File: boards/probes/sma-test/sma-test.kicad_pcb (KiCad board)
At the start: 4 copper layers, 45.6 x 44.1 mm, 6 parts, among them J1 901-10511-3, J2 901-10510-2, J3 901-10309, J4 901-10511-3, J5 901-10510-2, J6 901-10309

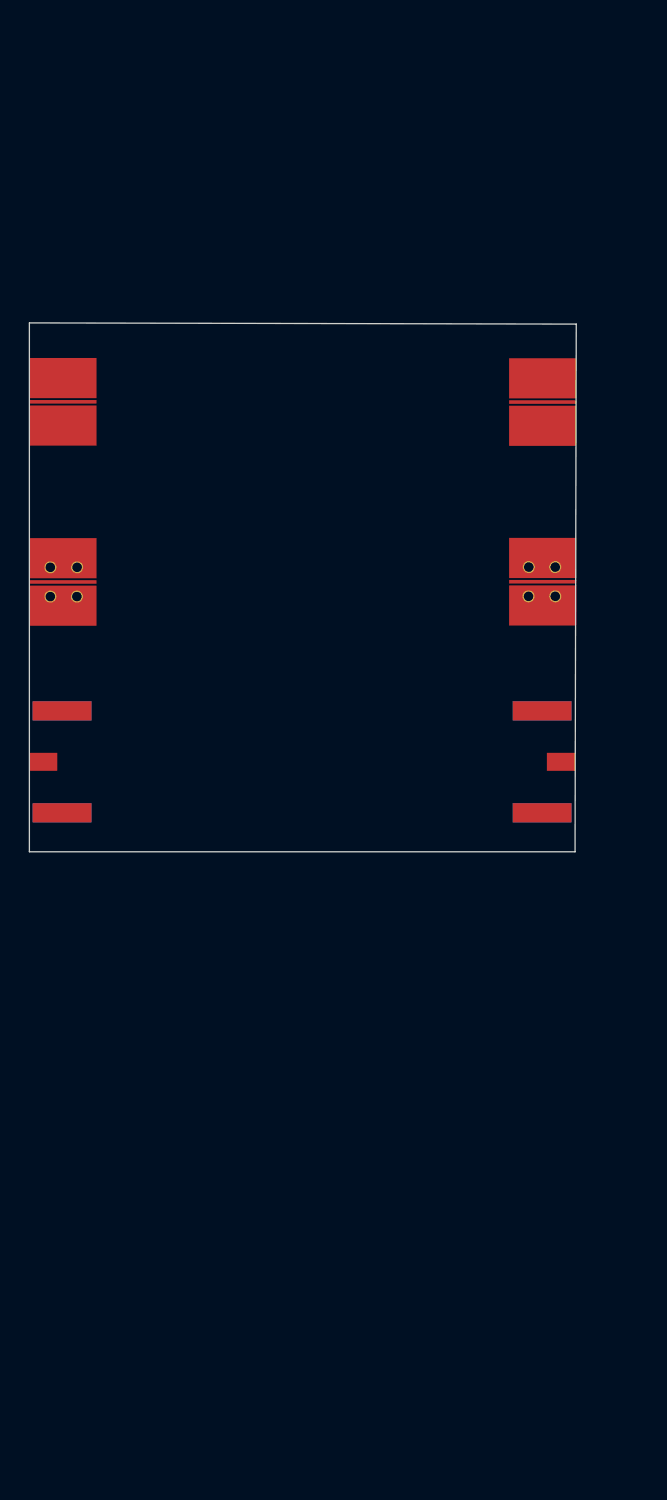
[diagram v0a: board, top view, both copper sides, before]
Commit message: Final version of sma-test board for fab
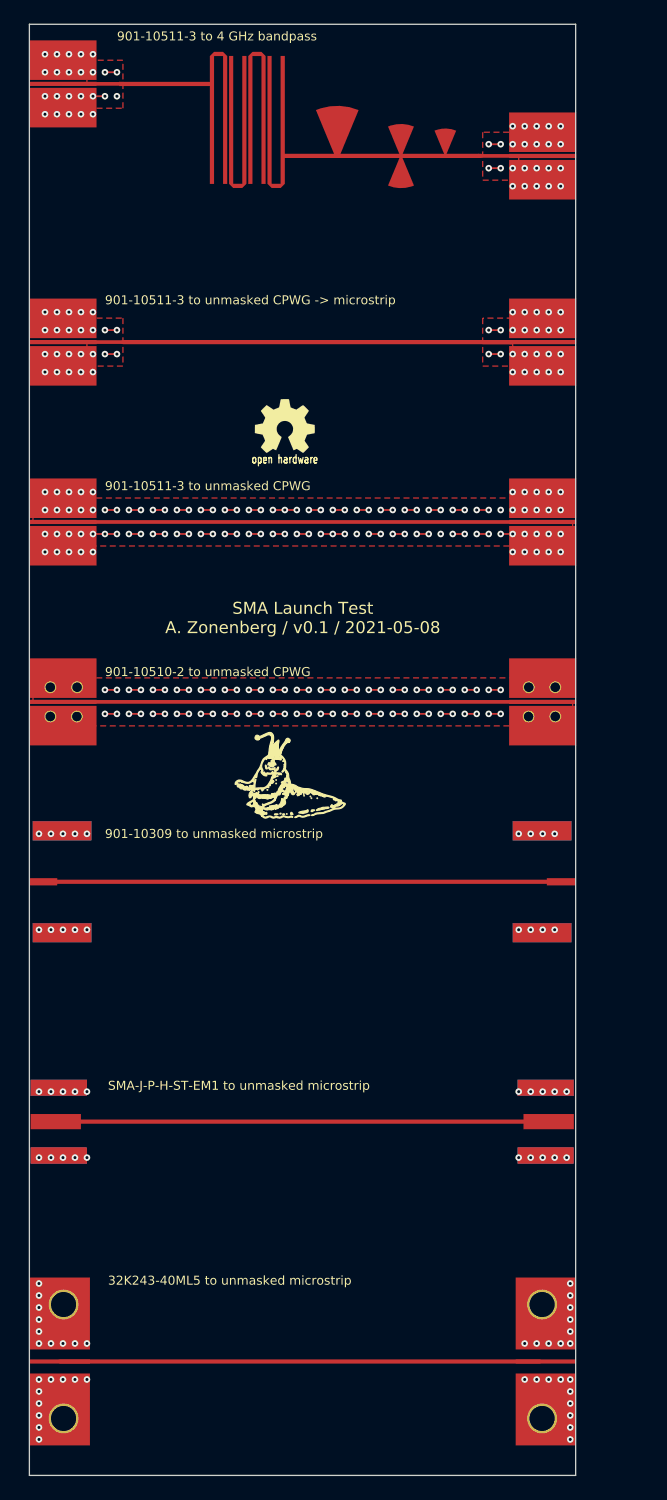
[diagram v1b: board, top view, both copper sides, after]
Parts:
- added FL1: FILTER, sma-test:filter2, F.Cu at (69.0, 29.8)
- added G***: LOGO, azonenberg_pcb:LONGTHING-1200DPI, F.Cu at (70.0, 82.0)
- added G***: LOGO, w_logo:Logo_silk_OSHW_6x6mm, F.Cu at (69.0, 52.5)
- added J10: 901-10511-3, azonenberg_pcb:CONN_SMA_EDGE_AMPHENOL_901_10511_3, F.Cu at (50.5, 24.0)
- added J11: SMA-J-P-H-ST-EM1, azonenberg_pcb:CONN_SMA_EDGE_SAMTEC_SMA_J_P_H_ST_EM1, F.Cu at (47.8, 110.5)
- added J12: 32K243-40ML5, azonenberg_pcb:CONN_SMA_EDGE_ROSENBERGER_32K243_40ML5, F.Cu at (47.8, 130.5)
- added J13: SMA-J-P-H-ST-EM1, azonenberg_pcb:CONN_SMA_EDGE_SAMTEC_SMA_J_P_H_ST_EM1, F.Cu at (93.1, 110.5)
- added J14: 32K243-40ML5, azonenberg_pcb:CONN_SMA_EDGE_ROSENBERGER_32K243_40ML5, F.Cu at (93.2, 130.5)
- added J7: 901-10511-3, azonenberg_pcb:CONN_SMA_EDGE_AMPHENOL_901_10511_3, F.Cu at (50.5, 45.5)
- added J8: 901-10511-3, azonenberg_pcb:CONN_SMA_EDGE_AMPHENOL_901_10511_3, F.Cu at (90.5, 45.5)
- added J9: 901-10511-3, azonenberg_pcb:CONN_SMA_EDGE_AMPHENOL_901_10511_3, F.Cu at (90.5, 30.0)
- moved J5 10.0 mm to (93.3, 75.5)
- moved J1 10.0 mm to (50.5, 60.5)
- moved J2 10.0 mm to (47.7, 75.5)
- moved J3 10.0 mm to (47.7, 90.5)
- moved J4 10.0 mm to (90.5, 60.5)
- moved J6 10.0 mm to (93.2, 90.5)
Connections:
- J2 pad 1: /SIG1 -> /SIG2
- J3 pad 1: /SIG1 -> /SIG3
- J5 pad 1: /SIG1 -> /SIG2
- J6 pad 1: /SIG1 -> /SIG3
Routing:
- net /GND: track 0.00 -> 724.6 mm, vias 0 -> 350
- net /SIG4: track 0.00 -> 45.0 mm
- net /SIG3: track 0.00 -> 43.2 mm
- net /SIG6: track 0.00 -> 41.1 mm
- net /SIG1: track 0.00 -> 41.0 mm
- net /SIG7: track 0.00 -> 40.0 mm
- net /SIG2: track 0.00 -> 40.0 mm
- net /SIG5: track 0.00 -> 5.25 mm
- net /SIG5B: track 0.00 -> 4.88 mm
- added copper zone on F.Cu, net /GND
- added copper zone on In1.Cu, net /GND
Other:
- board size 45.6 x 44.1 mm -> 45.5 x 121 mm
- board text added: "32K243-40ML5 to unmasked microstrip"
- board text added: "901-10309 to unmasked microstrip"
- board text added: "901-10510-2 to unmasked CPWG"
- board text added: "901-10511-3 to 4 GHz bandpass"
- board text added: "901-10511-3 to unmasked CPWG"
- board text added: "901-10511-3 to unmasked CPWG -> microstrip"
- board text added: "SMA Launch Test A. Zonenberg / v0.1 / 2021-05-08"
- board text added: "SMA-J-P-H-ST-EM1 to unmasked microstrip"

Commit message: Updated sma-test board with new cutouts and Beatty standard
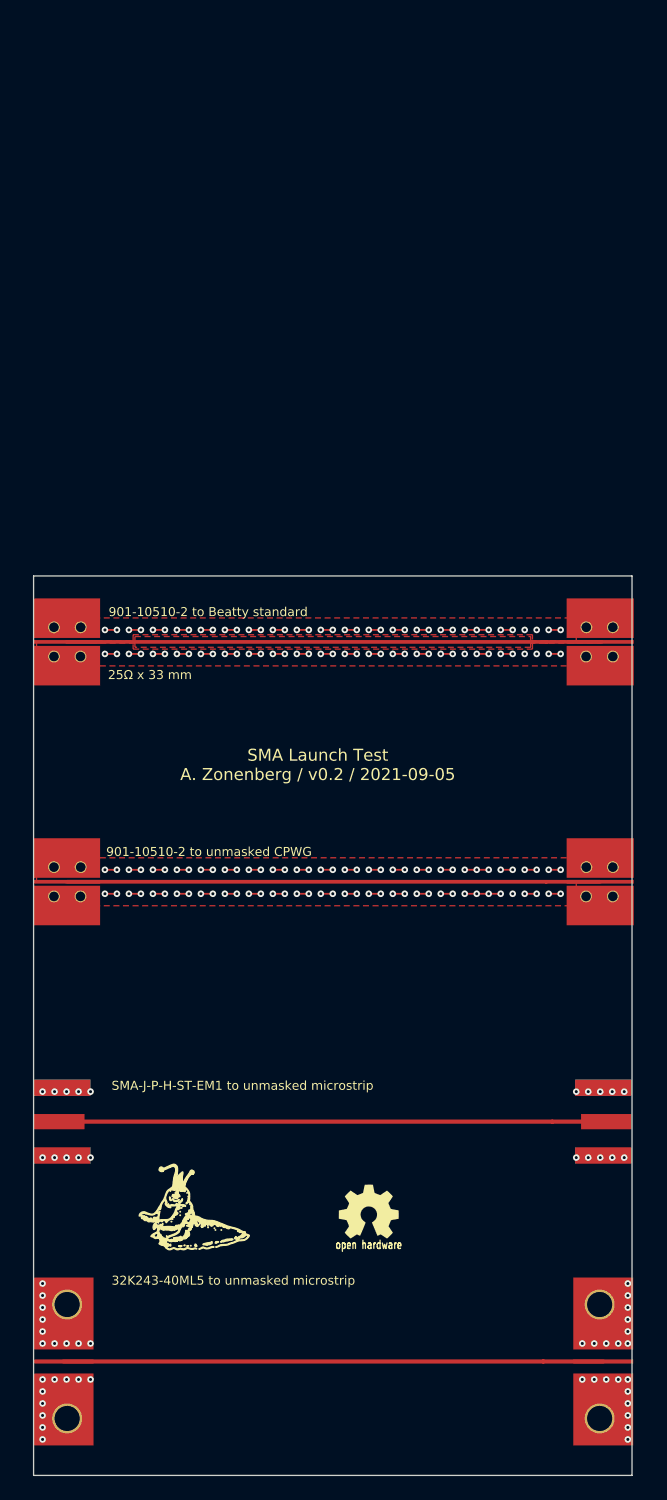
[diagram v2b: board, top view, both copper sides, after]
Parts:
- removed FL1: FILTER, sma-test:filter2
- removed J10, J4, J7, J8, J9: 901-10511-3, azonenberg_pcb:CONN_SMA_EDGE_AMPHENOL_901_10511_3
- removed J6: 901-10309, azonenberg_pcb:CONN_SMA_EDGE_AMPHENOL_901_10309
- J1: value 901-10511-3 -> 901-10510-2; footprint azonenberg_pcb:CONN_SMA_EDGE_AMPHENOL_901_10511_3 -> azonenberg_pcb:CONN_SMA_EDGE_AMPHENOL_901_10510-2
- J3: value 901-10309 -> 901-10510-2; footprint azonenberg_pcb:CONN_SMA_EDGE_AMPHENOL_901_10309 -> azonenberg_pcb:CONN_SMA_EDGE_AMPHENOL_901_10510-2
- moved G*** 65.9 mm to (76.0, 118.0)
- moved J3 54.2 mm to (98.1, 70.5), turned to 180 degrees
- moved G*** 36.9 mm to (62.0, 118.0)
- moved J5 15.7 mm to (98.1, 90.5)
- moved J2 15.0 mm to (48.0, 90.5)
- moved J1 10.3 mm to (48.0, 70.5)
- moved J13 4.80 mm to (97.9, 110.5)
- moved J14 4.80 mm to (98.0, 130.5)
- moved J11 0.30 mm to (48.1, 110.5)
- moved J12 0.30 mm to (48.0, 130.5)
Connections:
- J3 pad 1: /SIG3 -> /SIG1
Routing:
- net /GND: track 724.6 -> 426.8 mm, vias 350 -> 216
- net /SIG4: track 45.0 -> 0.00 mm
- net /SIG3: track 43.2 -> 0.00 mm
- net /SIG5: track 5.25 -> 0.00 mm
- net /SIG7: track 40.0 -> 45.0 mm
- net /SIG5B: track 4.88 -> 0.00 mm
- net /SIG2: track 40.0 -> 44.5 mm
- net /SIG6: track 41.1 -> 45.6 mm
- net /SIG1: track 41.0 -> 44.5 mm
- added copper zone on F.Cu, net /SIG1
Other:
- board size 45.5 x 121 mm -> 49.9 x 75 mm
- board text added: "25Ω x 33 mm"
- board text added: "901-10510-2 to Beatty standard"
- board text added: "SMA Launch Test A. Zonenberg / v0.2 / 2021-09-05"
- board text removed: "901-10309 to unmasked microstrip"
- board text removed: "901-10511-3 to 4 GHz bandpass"
- board text removed: "901-10511-3 to unmasked CPWG"
- board text removed: "901-10511-3 to unmasked CPWG -> microstrip"
- board text removed: "SMA Launch Test A. Zonenberg / v0.1 / 2021-05-08"

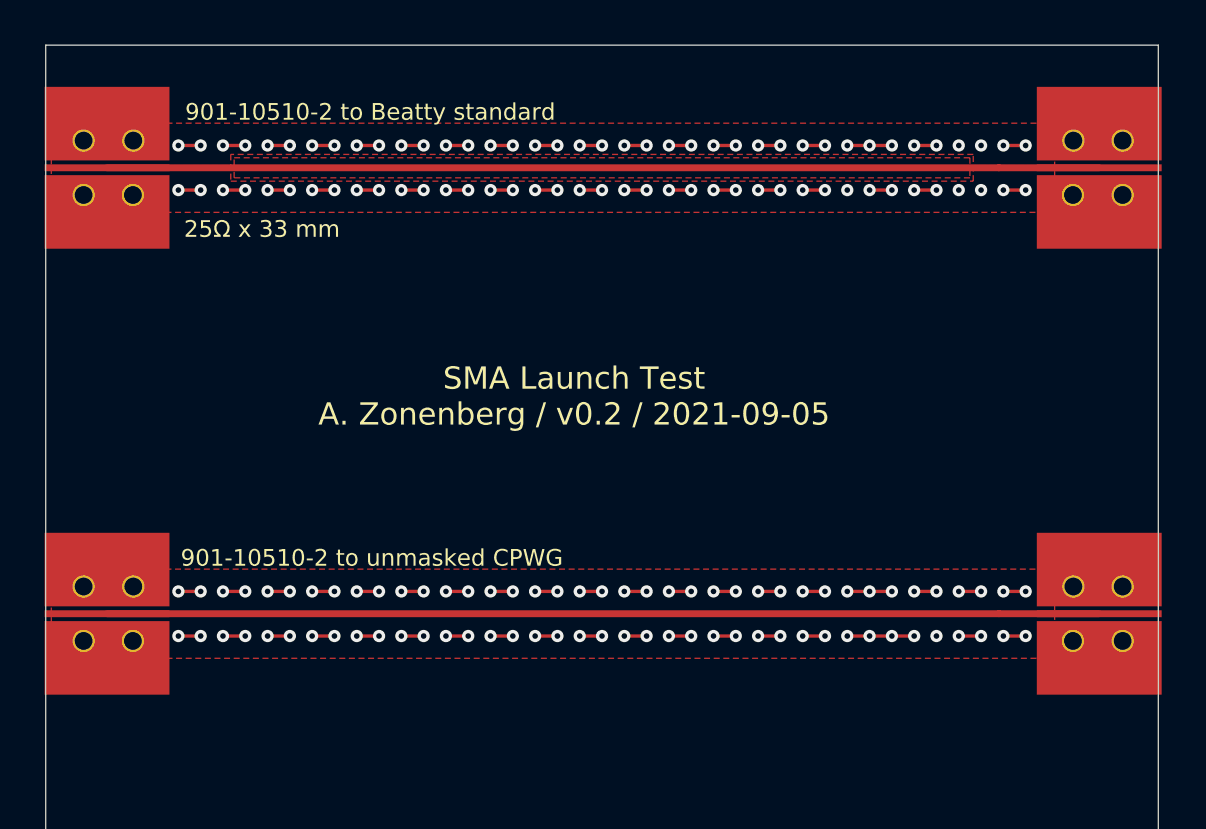
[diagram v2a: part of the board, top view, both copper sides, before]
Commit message: Updated 901-10510-2 with latest footprint from library. Added more vias to connector field
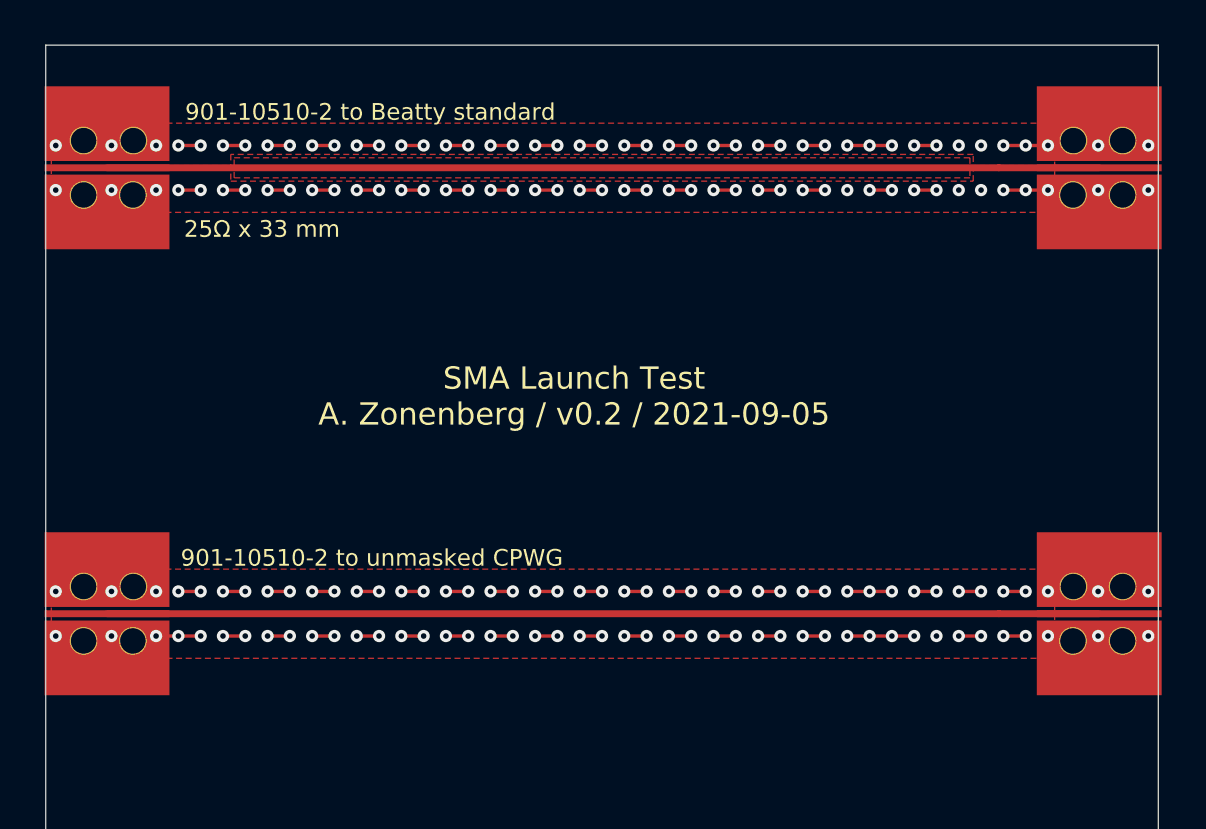
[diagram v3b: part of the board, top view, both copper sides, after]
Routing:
- net /GND: track 426.8 -> 459.4 mm, vias 216 -> 240

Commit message: Missing change from last commit
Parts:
- added J4: 901-10510-2, azonenberg_pcb:CONN_SMA_EDGE_AMPHENOL_901_10510-2, F.Cu at (47.2, 50.5)
- added J6: 901-10510-2, azonenberg_pcb:CONN_SMA_EDGE_AMPHENOL_901_10510-2, F.Cu at (98.8, 50.5)
- added R1: R, azonenberg_pcb:EIA_0402_RES_NOSILK, F.Cu at (73.0, 50.5)
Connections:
- net /SIG6 renamed /SIG3
- net /SIG7 renamed /SIG4
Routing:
- net /GND: track 459.4 -> 575.3 mm, vias 240 -> 334
- net /SIG5B: track 0.00 -> 22.5 mm
- net /SIG5A: track 0.00 -> 21.8 mm
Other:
- board size 49.9 x 75 mm -> 51.4 x 95 mm
- board text added: "2x thru for 0402"
- board text added: "901-10510-2 to 0402"
- board text added: "SMA Launch Test A. Zonenberg / v0.2 / 2021-09-06"
- board text removed: "SMA Launch Test A. Zonenberg / v0.2 / 2021-09-05"
